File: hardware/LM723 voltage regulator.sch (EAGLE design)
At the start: 41 parts, among them IC1 LM358, J1 CON_TERMINAL_BLOCK_02-5MM, J2 CON_TERMINAL_BLOCK_02-5MM, J3 CON_HEADER_1X03-PTH, Q1 2SA1015, Q2 2N3904, Q3 2N3055, Q4 2SA1015, U1 LM723-EXPAD

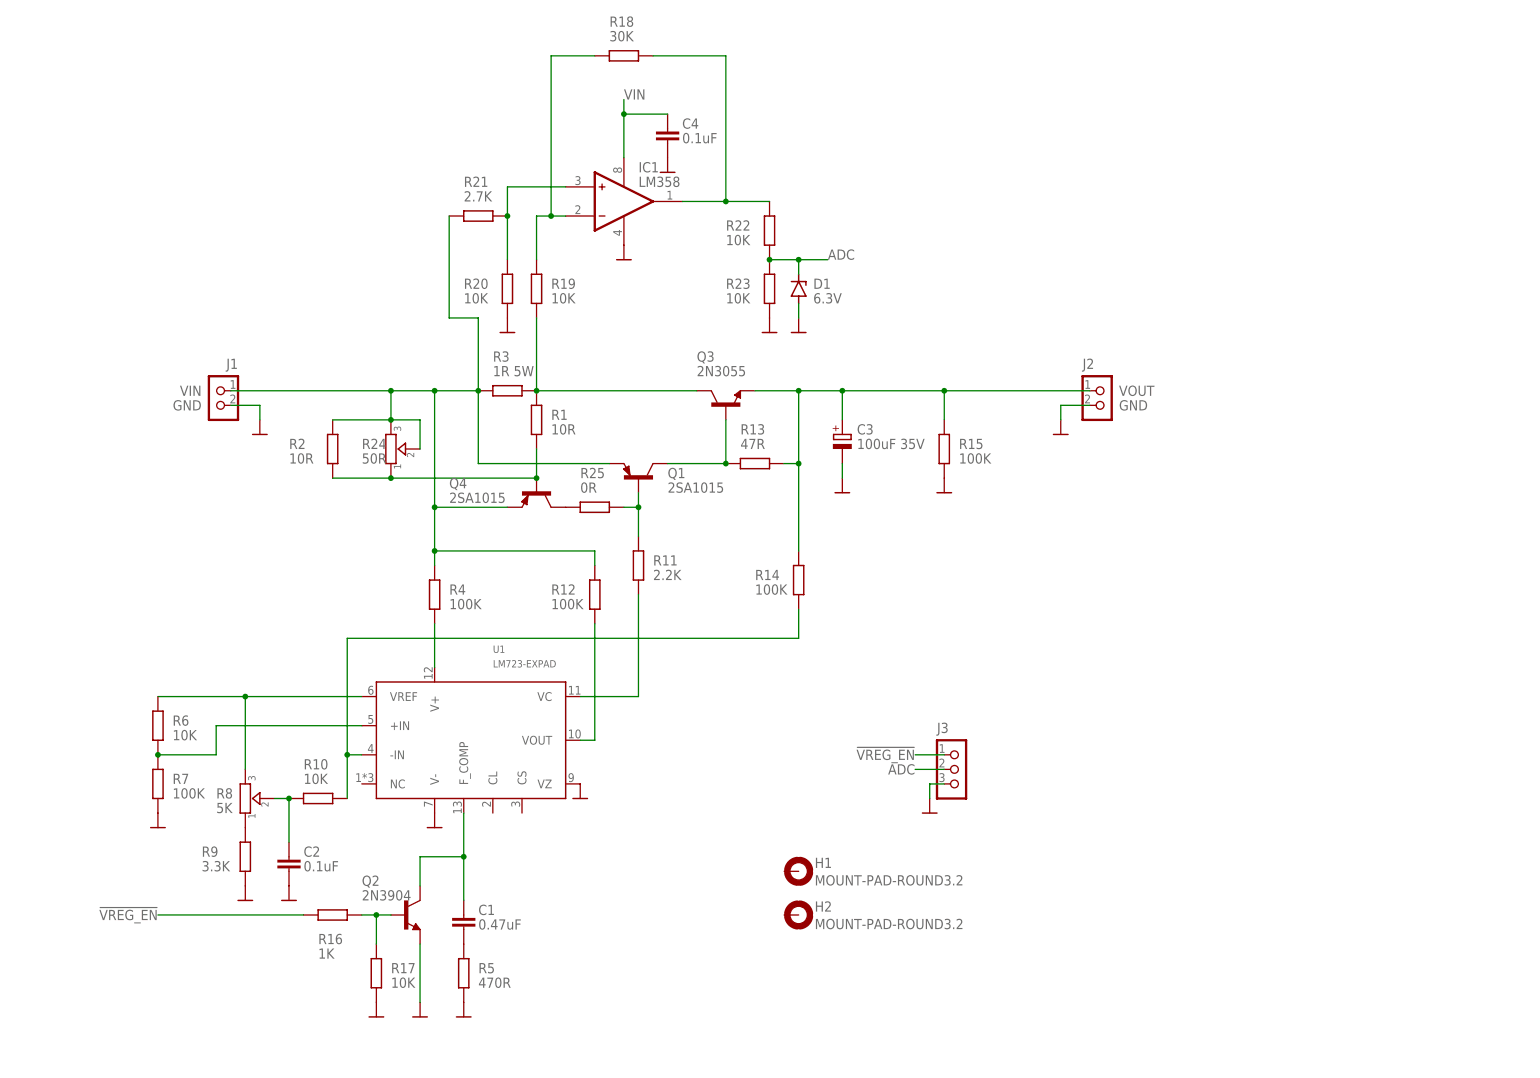
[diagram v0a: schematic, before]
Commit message: fix circuit and made 2 panelized board
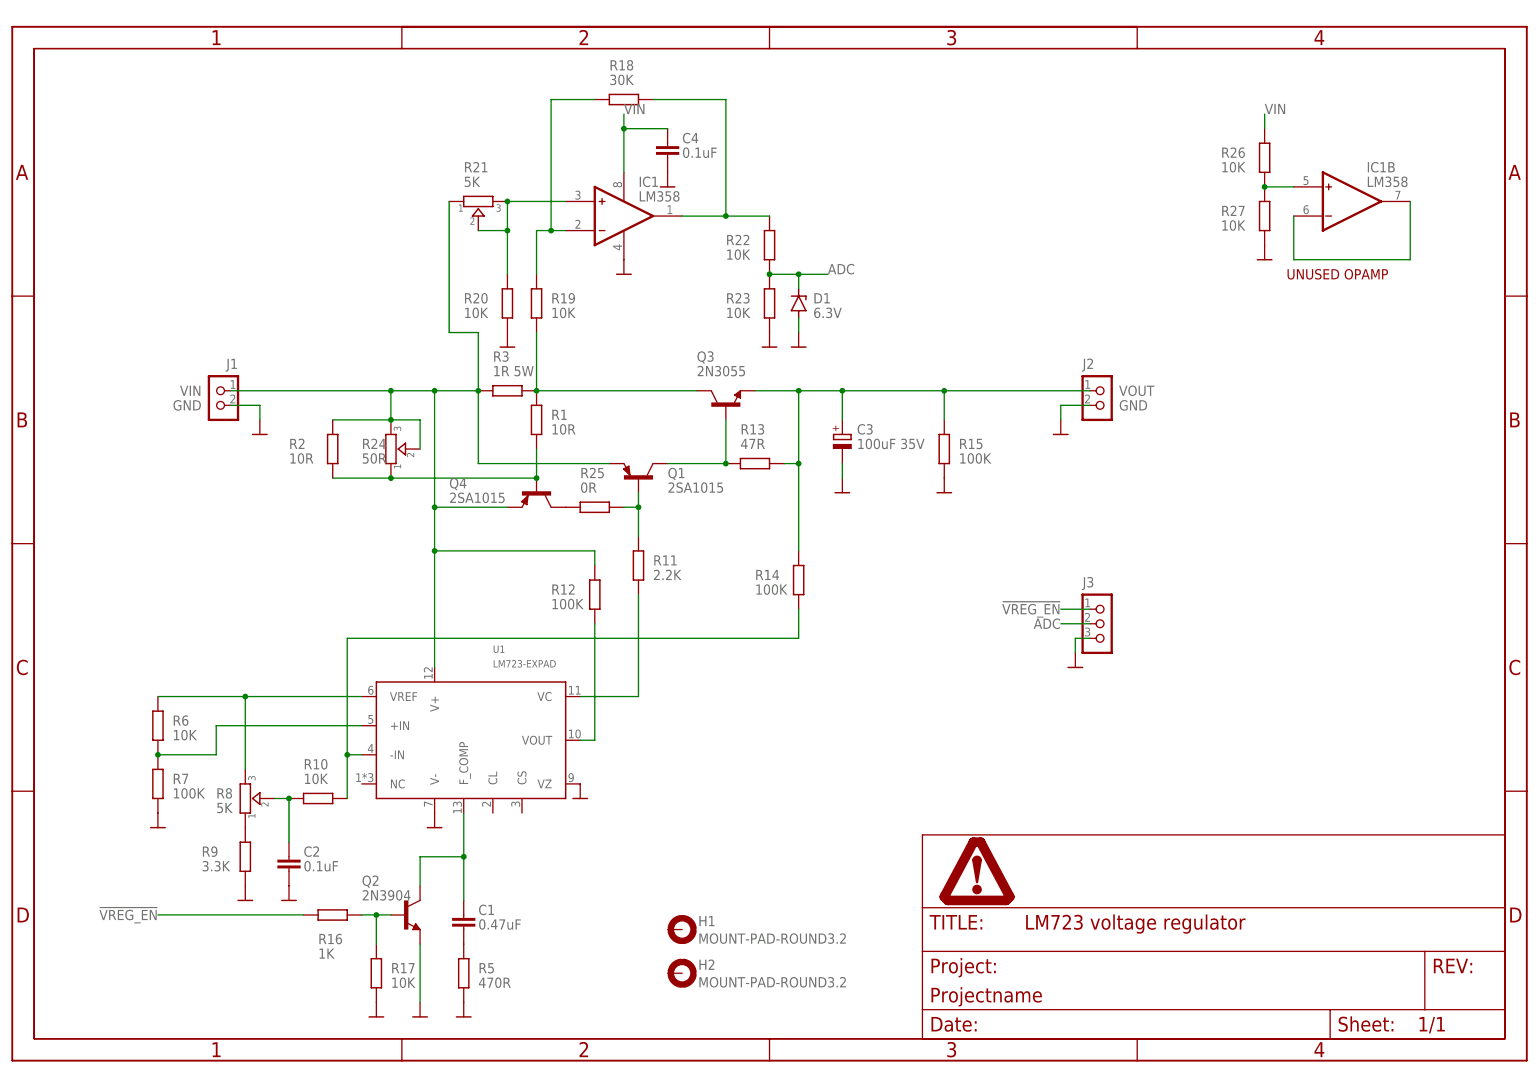
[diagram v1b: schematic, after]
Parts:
- removed R4: 100K, trosh_devices.eagle.v9:RESISTOR-V
- added PAGE1: FRAME_DINA4_L, dp_devices.v6:FRAME_DINA4_L
- added R26, R27: 10K, trosh_devices.eagle.v9:RESISTOR-V
- R21: value 2.7K -> 5K; device trosh_devices.eagle.v9:RESISTOR -> trosh_devices.eagle.v9:TRIMMER-3362P_EXPAD
- R24, R8: device dp_devices.v6:TRIMMER-3362P -> trosh_devices.eagle.v9:TRIMMER-3362P_EXPAD
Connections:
- removed net N$5: R4.1, U1.V+
- new net N$20: IC1B.-, IC1B.OUT
- new net N$21: IC1B.+, R26.2, R27.1
- net GND: now also R27.2
- net N$16: now also R21.3
- net VIN: now also R26.1, U1.V+; no longer R4.2
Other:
- note added: "UNUSED OPAMP"
- moved on the sheet: C4, D1, H1, H2, IC1, J3, R18, R19, R20, R22, R23

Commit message: finish routing main board and bom
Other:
- note added: "change to SO8"
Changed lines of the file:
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@@
 <text x="9.652" y="36.068" size="1.778" layer="98">Vref = 7.15V</text>
 <text x="193.04" y="109.22" size="1.778" layer="94" align="center">UNUSED OPAMP</text>
+<text x="57.912" y="127.508" size="1.778" layer="98">change to SO8</text>
 </plain>
 <instances>
